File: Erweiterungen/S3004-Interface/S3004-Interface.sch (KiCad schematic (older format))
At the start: 15 parts

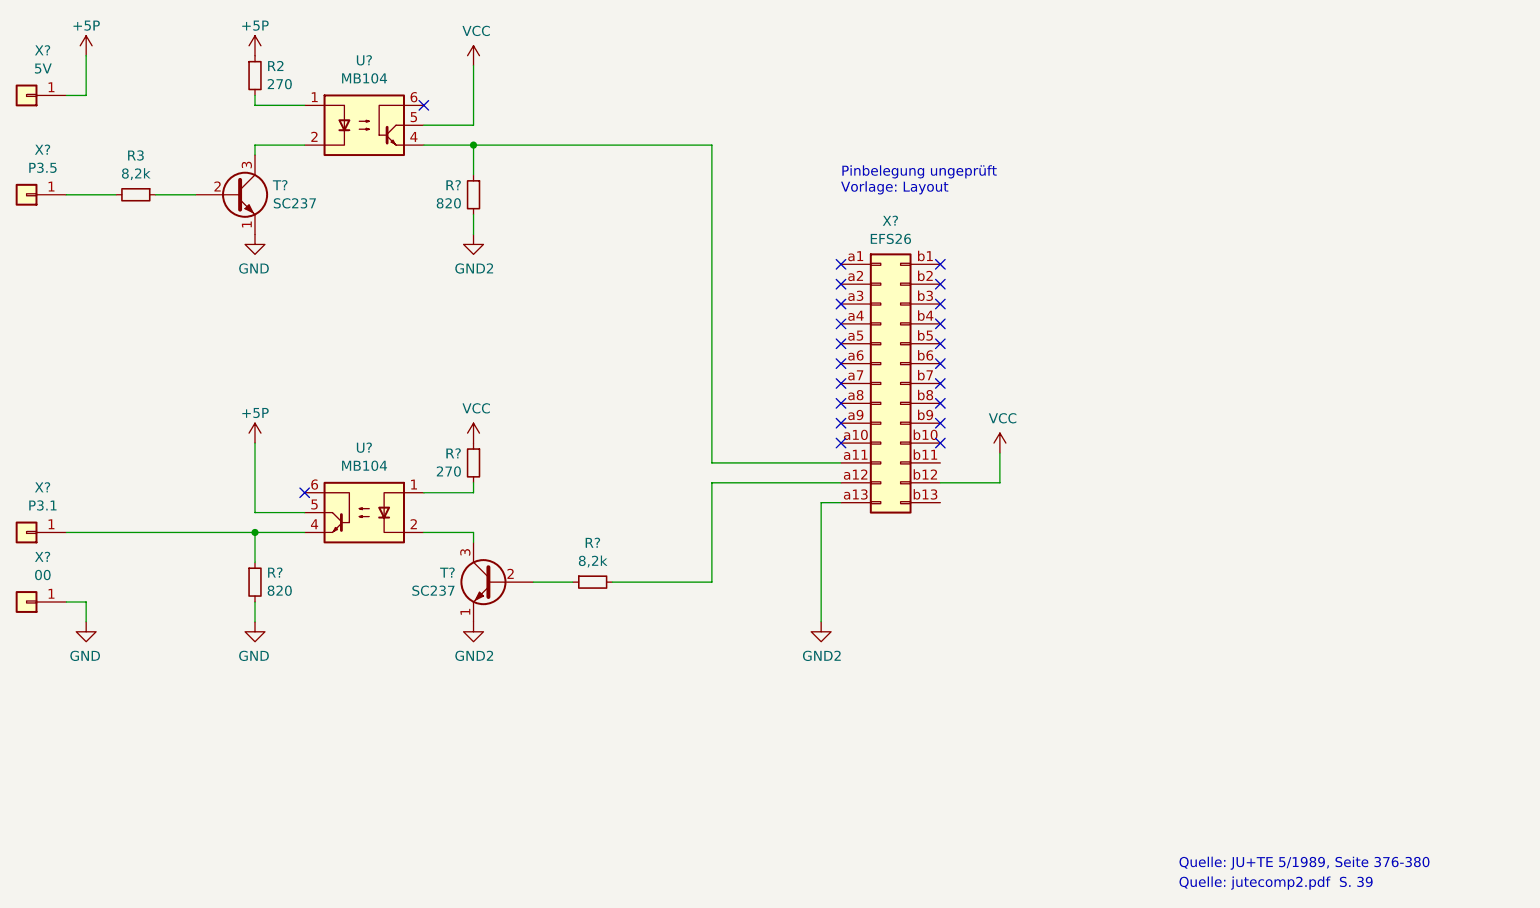
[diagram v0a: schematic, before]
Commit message: S3004-Interface präzisiert (und annotiert)
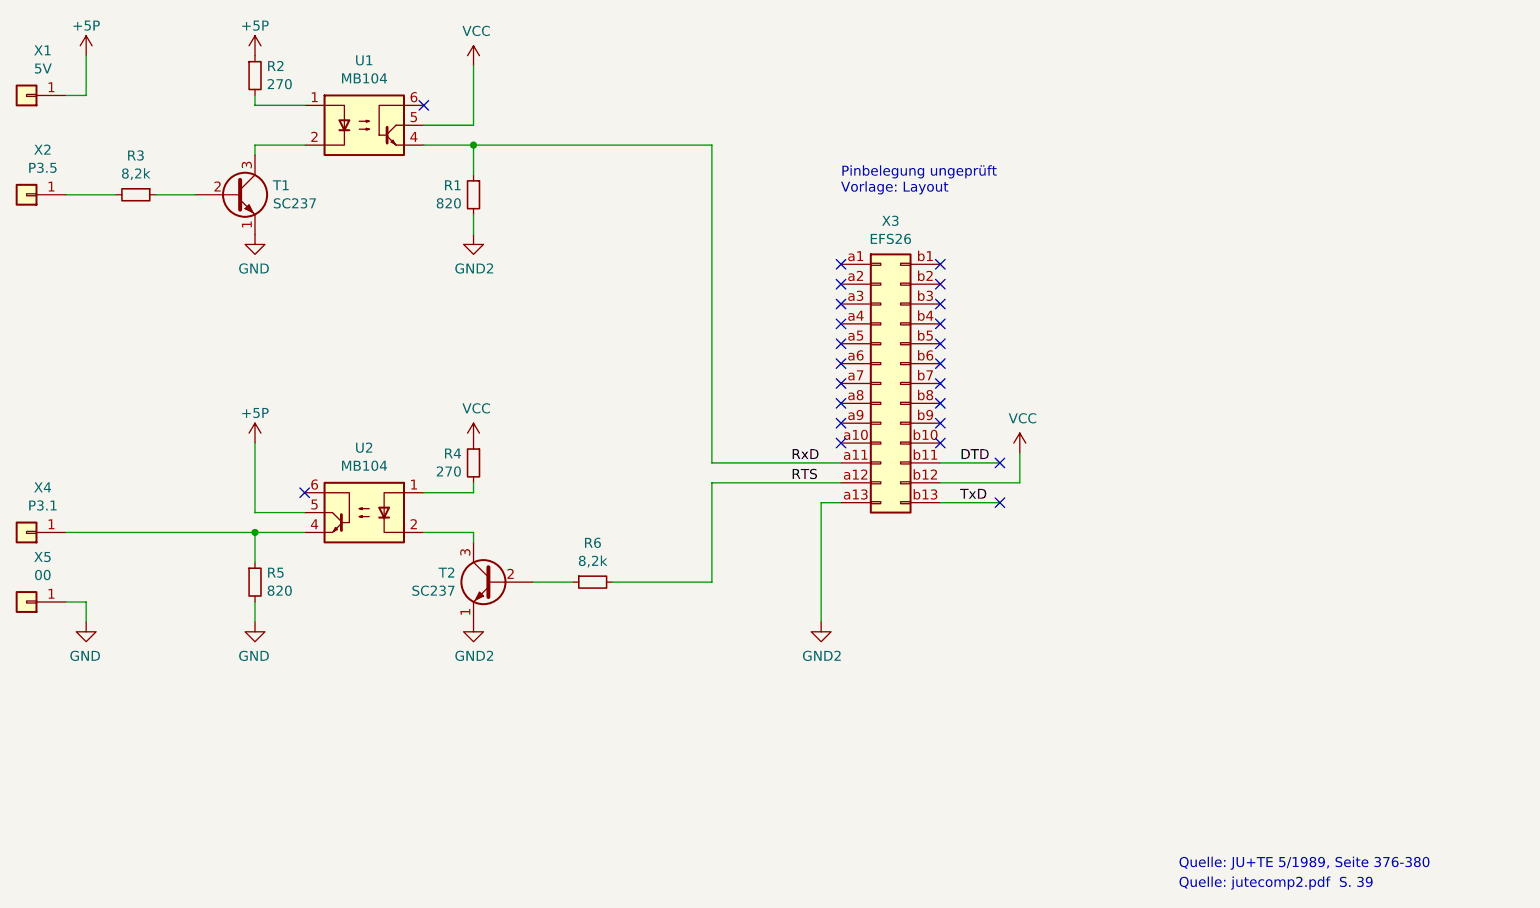
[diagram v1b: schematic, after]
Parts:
- gave numbers to parts that had none: 13
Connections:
- net RxD: now reaches R1.1, U1.4, X3.a11 (Pin_a11)
- net RTS: now reaches R6.2, X3.a12 (Pin_a12)
- net DTD: now reaches X3.b11 (Pin_b11)
- net TxD: now reaches X3.b13 (Pin_b13)
- no-connect marks 22 -> 24
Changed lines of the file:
@@
 Sheet 1 1
 Title "Interface für Erika S3004"
-Date "5.12.21"
-Rev "1"
+Date "14.12.21"
+Rev "2"
 Comp "Jugend+Technik"
 Comment1 "Bert"
@@
 	5300 3000 5300 3050
 $Comp
-L RFT_Optoelektronik:MB104 U?
+L RFT_Optoelektronik:MB104 U1
 U 1 1 61AD55FC
 P 5850 3150
-F 0 "U?" H 5850 3475 50  0000 C CNN
+F 0 "U1" H 5850 3475 50  0000 C CNN
 F 1 "MB104" H 5850 3384 50  0000 C CNN
 F 2 "Package_DIP:DIP-6_W7.62mm" H 5850 2850 50  0001 C CNN
@@
 $EndComp
 $Comp
-L RFT_Optoelektronik:MB104 U?
+L RFT_Optoelektronik:MB104 U2
 U 1 1 61AD74F5
 P 5850 5100
-F 0 "U?" H 5850 5425 50  0000 C CNN
+F 0 "U2" H 5850 5425 50  0000 C CNN
 F 1 "MB104" H 5850 5334 50  0000 C CNN
 F 2 "Package_DIP:DIP-6_W7.62mm" H 5850 4800 50  0001 C CNN
@@
 $EndComp
 $Comp
-L RFT_Transistoren_und_Dioden:SC237 T?
+L RFT_Transistoren_und_Dioden:SC237 T1
 U 1 1 61AD9D26
 P 5200 3500
-F 0 "T?" H 5390 3546 50  0000 L CNN
+F 0 "T1" H 5390 3546 50  0000 L CNN
 F 1 "SC237" H 5390 3455 50  0000 L CNN
 F 2 "" H 5250 3500 50  0001 C CNN
@@
 	4600 3500 4350 3500
 $Comp
-L Connector_Generic:Conn_01x01 X?
+L Connector_Generic:Conn_01x01 X2
 U 1 1 61AF55FD
 P 4150 3500
-F 0 "X?" H 4068 3275 50  0000 C CNN
+F 0 "X2" H 4068 3275 50  0000 C CNN
 F 1 "P3.5" H 4068 3366 50  0000 C CNN
 F 2 "" H 4150 3500 50  0001 C CNN
@@
 AR Path="/60FD40F8/61AFD984" Ref="#PWR?"  Part="1"
 AR Path="/61282124/61AFD984" Ref="#PWR?"  Part="1"
-AR Path="/61AFD984" Ref="#PWR?"  Part="1"
-F 0 "#PWR?" H 5300 5400 50  0001 C CNN
+AR Path="/61AFD984" Ref="#PWR09"  Part="1"
+F 0 "#PWR09" H 5300 5400 50  0001 C CNN
 F 1 "GND" H 5305 5477 50  0000 C CNN
 F 2 "" H 5300 5650 50  0001 C CNN
@@
 AR Path="/60FD40F8/61AFDDB5" Ref="#PWR?"  Part="1"
 AR Path="/61282124/61AFDDB5" Ref="#PWR?"  Part="1"
-AR Path="/61AFDDB5" Ref="#PWR?"  Part="1"
-F 0 "#PWR?" H 5300 4600 50  0001 C CNN
+AR Path="/61AFDDB5" Ref="#PWR05"  Part="1"
+F 0 "#PWR05" H 5300 4600 50  0001 C CNN
 F 1 "+5P" H 5300 4900 50  0000 C CNN
 F 2 "" H 5300 4750 50  0001 C CNN
@@
 $EndComp
 $Comp
-L Device:R_Small R?
+L Device:R_Small R5
 U 1 1 61AFE10B
 P 5300 5450
-F 0 "R?" H 5359 5496 50  0000 L CNN
+F 0 "R5" H 5359 5496 50  0000 L CNN
 F 1 "820" H 5359 5405 50  0000 L CNN
 F 2 "" H 5300 5450 50  0001 C CNN
@@
 	5300 5550 5300 5650
 $Comp
-L Connector_Generic:Conn_01x01 X?
+L Connector_Generic:Conn_01x01 X4
 U 1 1 61B03D08
 P 4150 5200
-F 0 "X?" H 4068 4975 50  0000 C CNN
+F 0 "X4" H 4068 4975 50  0000 C CNN
 F 1 "P3.1" H 4068 5066 50  0000 C CNN
 F 2 "" H 4150 5200 50  0001 C CNN
@@
 	5300 5100 5300 4750
 $Comp
-L power:VCC #PWR?
+L power:VCC #PWR06
 U 1 1 61B0A5DA
 P 6400 4750
-F 0 "#PWR?" H 6400 4600 50  0001 C CNN
+F 0 "#PWR06" H 6400 4600 50  0001 C CNN
 F 1 "VCC" H 6415 4923 50  0000 C CNN
 F 2 "" H 6400 4750 50  0001 C CNN
@@
 $EndComp
 $Comp
-L Device:R_Small R?
+L Device:R_Small R6
 U 1 1 61B0B64C
 P 7000 5450
-F 0 "R?" V 6804 5450 50  0000 C CNN
+F 0 "R6" V 6804 5450 50  0000 C CNN
 F 1 "8,2k" V 6895 5450 50  0000 C CNN
 F 2 "" H 7000 5450 50  0001 C CNN
@@
 $EndComp
 $Comp
-L Device:R_Small R?
+L Device:R_Small R4
 U 1 1 61B0B656
 P 6400 4850
-F 0 "R?" H 6459 4896 50  0000 L CNN
+F 0 "R4" H 6459 4896 50  0000 L CNN
 F 1 "270" H 6459 4805 50  0000 L CNN
 F 2 "" H 6400 4850 50  0001 C CNN
@@
 	6400 4950 6400 5000
 $Comp
-L RFT_Transistoren_und_Dioden:SC237 T?
+L RFT_Transistoren_und_Dioden:SC237 T2
 U 1 1 61B0B66C
 P 6500 5450
-F 0 "T?" H 6690 5496 50  0000 L CNN
+F 0 "T2" H 6690 5496 50  0000 L CNN
 F 1 "SC237" H 6690 5405 50  0000 L CNN
 F 2 "" H 6550 5450 50  0001 C CNN
@@
 	6700 5450 6900 5450
 $Comp
-L Device:R_Small R?
+L Device:R_Small R1
 U 1 1 61B19A27
 P 6400 3500
-F 0 "R?" H 6459 3546 50  0000 L CNN
+F 0 "R1" H 6459 3546 50  0000 L CNN
 F 1 "820" H 6459 3455 50  0000 L CNN
 F 2 "" H 6400 3500 50  0001 C CNN
@@
 	6400 3150 6400 2850
 $Comp
-L power:VCC #PWR?
+L power:VCC #PWR03
 U 1 1 61B36F36
 P 6400 2850
-F 0 "#PWR?" H 6400 2700 50  0001 C CNN
+F 0 "#PWR03" H 6400 2700 50  0001 C CNN
 F 1 "VCC" H 6415 3023 50  0000 C CNN
 F 2 "" H 6400 2850 50  0001 C CNN
@@
 $EndComp
 $Comp
-L Connector_Generic:Conn_02x13_Row_Letter_First X?
+L Connector_Generic:Conn_02x13_Row_Letter_First X3
 U 1 1 61B37DBE
 P 8450 4450
-F 0 "X?" H 8500 5267 50  0000 C CNN
+F 0 "X3" H 8500 5267 50  0000 C CNN
 F 1 "EFS26" H 8500 5176 50  0000 C CNN
 F 2 "" H 8450 4450 50  0001 C CNN
@@
 $EndComp
 $Comp
-L Connector_Generic:Conn_01x01 X?
+L Connector_Generic:Conn_01x01 X1
 U 1 1 61B60003
 P 4150 3000
-F 0 "X?" H 4068 2775 50  0000 C CNN
+F 0 "X1" H 4068 2775 50  0000 C CNN
 F 1 "5V" H 4068 2866 50  0000 C CNN
 F 2 "" H 4150 3000 50  0001 C CNN
@@
 AR Path="/60FD40F8/61B60456" Ref="#PWR?"  Part="1"
 AR Path="/61282124/61B60456" Ref="#PWR?"  Part="1"
-AR Path="/61B60456" Ref="#PWR?"  Part="1"
-F 0 "#PWR?" H 4450 2650 50  0001 C CNN
+AR Path="/61B60456" Ref="#PWR01"  Part="1"
+F 0 "#PWR01" H 4450 2650 50  0001 C CNN
 F 1 "+5P" H 4450 2950 50  0000 C CNN
 F 2 "" H 4450 2800 50  0001 C CNN
@@
 	4450 3000 4450 2800
 $Comp
-L Connector_Generic:Conn_01x01 X?
+L Connector_Generic:Conn_01x01 X5
 U 1 1 61B64012
 P 4150 5550
-F 0 "X?" H 4068 5325 50  0000 C CNN
+F 0 "X5" H 4068 5325 50  0000 C CNN
 F 1 "00" H 4068 5416 50  0000 C CNN
 F 2 "" H 4150 5550 50  0001 C CNN
@@
 AR Path="/60FD40F8/61B641E6" Ref="#PWR?"  Part="1"
 AR Path="/61282124/61B641E6" Ref="#PWR?"  Part="1"
-AR Path="/61B641E6" Ref="#PWR?"  Part="1"
-F 0 "#PWR?" H 4450 5400 50  0001 C CNN
+AR Path="/61B641E6" Ref="#PWR08"  Part="1"
+F 0 "#PWR08" H 4450 5400 50  0001 C CNN
 F 1 "GND" H 4455 5477 50  0000 C CNN
 F 2 "" H 4450 5650 50  0001 C CNN
@@
 	4450 5550 4350 5550
 $Comp
-L power:GND2 #PWR?
+L power:GND2 #PWR010
 U 1 1 61B687BB
 P 6400 5650
-F 0 "#PWR?" H 6400 5400 50  0001 C CNN
+F 0 "#PWR010" H 6400 5400 50  0001 C CNN
 F 1 "GND2" H 6405 5477 50  0000 C CNN
 F 2 "" H 6400 5650 50  0001 C CNN
@@
 $EndComp
 $Comp
-L power:GND2 #PWR?
+L power:GND2 #PWR04
 U 1 1 61B69227
 P 6400 3700
-F 0 "#PWR?" H 6400 3450 50  0001 C CNN
+F 0 "#PWR04" H 6400 3450 50  0001 C CNN
 F 1 "GND2" H 6405 3527 50  0000 C CNN
 F 2 "" H 6400 3700 50  0001 C CNN
@@
 $EndComp
 $Comp
-L power:GND2 #PWR?
+L power:GND2 #PWR011
 U 1 1 61B6957F
 P 8150 5650
-F 0 "#PWR?" H 8150 5400 50  0001 C CNN
+F 0 "#PWR011" H 8150 5400 50  0001 C CNN
 F 1 "GND2" H 8155 5477 50  0000 C CNN
 F 2 "" H 8150 5650 50  0001 C CNN
@@
 NoConn ~ 6150 3050
 $Comp
-L power:VCC #PWR?
+L power:VCC #PWR07
 U 1 1 61B7CDCA
-P 9050 4800
-F 0 "#PWR?" H 9050 4650 50  0001 C CNN
-F 1 "VCC" H 9065 4973 50  0000 C CNN
-F 2 "" H 9050 4800 50  0001 C CNN
-F 3 "" H 9050 4800 50  0001 C CNN
-	1    9050 4800
-	1    0    0    -1
-$EndComp
-Wire Wire Line
-	8750 4950 9050 4950
-Wire Wire Line
-	9050 4950 9050 4800
+P 9150 4800
+F 0 "#PWR07" H 9150 4650 50  0001 C CNN
+F 1 "VCC" H 9165 4973 50  0000 C CNN
+F 2 "" H 9150 4800 50  0001 C CNN
+F 3 "" H 9150 4800 50  0001 C CNN
+	1    9150 4800
+	1    0    0    -1
+$EndComp
+Wire Wire Line
+	8750 4950 9150 4950
+Wire Wire Line
+	9150 4950 9150 4800
 NoConn ~ 8250 4750
 NoConn ~ 8250 4650
@@
 Text Notes 8250 3500 0    50   ~ 0
 Pinbelegung ungeprüft\nVorlage: Layout
+Text Label 8000 4850 0    50   ~ 0
+RxD
+Text Label 8000 4950 0    50   ~ 0
+RTS
+Text Label 8850 5050 0    50   ~ 0
+TxD
+Text Label 8850 4850 0    50   ~ 0
+DTD
+Wire Wire Line
+	8750 4850 9050 4850
+Wire Wire Line
+	8750 5050 9050 5050
+NoConn ~ 9050 4850
+NoConn ~ 9050 5050
 $EndSCHEMATC
